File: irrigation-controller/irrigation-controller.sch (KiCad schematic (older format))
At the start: 31 parts, among them P1 CONN_1, P2 CONN_1, P3 CONN_1, P4 CONN_1, P5 CONN_1, P6 CONN_1, P7 CONN_1, P8 CONN_1, P9 PSUBOARD, Q1 IRF540, Q2 IRF540, Q3 IRF540, Q4 IRF540, Q5 IRF540

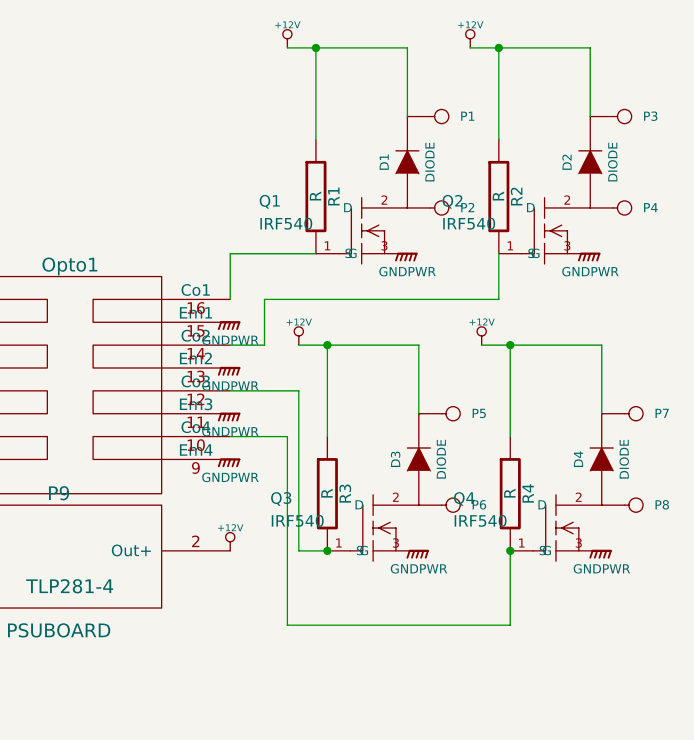
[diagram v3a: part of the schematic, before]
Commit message: Fix inverted behavior on high side
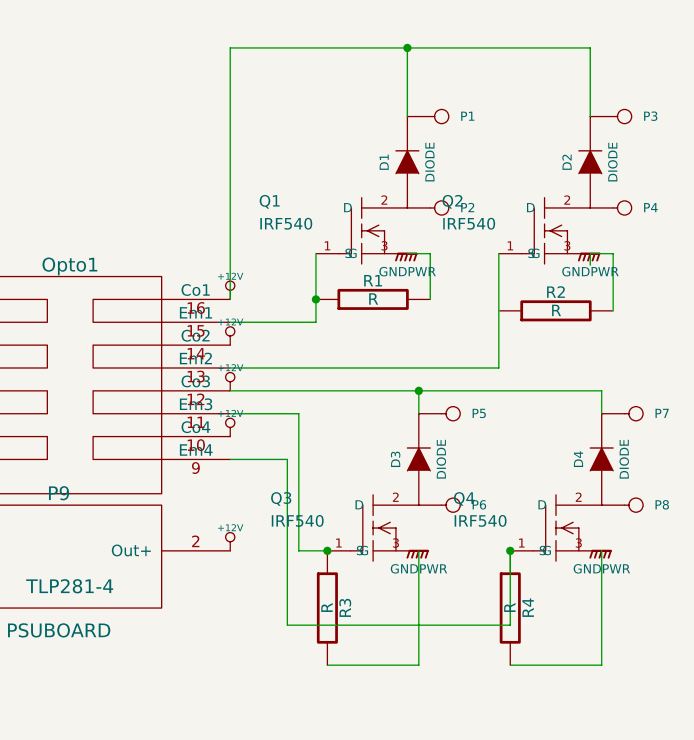
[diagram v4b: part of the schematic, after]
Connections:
- net +12V: now also Opto1.10 (Co4), Opto1.12 (Co3), Opto1.14 (Co2), Opto1.16 (Co1); no longer R1.1, R2.1, R3.1, R4.1
- net GNDPWR: now also R1.2, R2.2, R3.2, R4.2; no longer Opto1.11 (Em3), Opto1.13 (Em2), Opto1.15 (Em1), Opto1.9 (Em4)
- new net: Opto1.15 (Em1), Q1.1 (G), R1.1
- new net: Opto1.11 (Em3), Q3.1 (G), R3.1
- new net: Opto1.13 (Em2), Q2.1 (G)
- new net: Opto1.9 (Em4), Q4.1 (G), R4.1
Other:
- moved on the sheet: R1, R2, R3, R4
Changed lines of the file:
@@
-EESchema Schematic File Version 2  date 5/14/2014 8:58:33 PM
+EESchema Schematic File Version 2  date 6/8/2014 10:10:39 PM
 LIBS:power
 LIBS:device
@@
 Sheet 1 1
 Title ""
-Date "15 may 2014"
+Date "9 jun 2014"
 Rev ""
 Comp ""
@@
 Comment4 ""
 $EndDescr
-$Comp
-L GNDPWR #PWR?
-U 1 1 53741138
-P 9450 3650
-F 0 "#PWR?" H 9450 3700 40  0001 C CNN
-F 1 "GNDPWR" H 9450 3570 40  0000 C CNN
-	1    9450 3650
-	1    0    0    -1
-$EndComp
-$Comp
-L GNDPWR #PWR?
-U 1 1 53741137
-P 9450 3450
-F 0 "#PWR?" H 9450 3500 40  0001 C CNN
-F 1 "GNDPWR" H 9450 3370 40  0000 C CNN
-	1    9450 3450
-	1    0    0    -1
-$EndComp
-$Comp
-L GNDPWR #PWR?
-U 1 1 53741135
-P 9450 3250
-F 0 "#PWR?" H 9450 3300 40  0001 C CNN
-F 1 "GNDPWR" H 9450 3170 40  0000 C CNN
-	1    9450 3250
-	1    0    0    -1
-$EndComp
-$Comp
-L GNDPWR #PWR?
-U 1 1 53741133
-P 9450 3050
-F 0 "#PWR?" H 9450 3100 40  0001 C CNN
-F 1 "GNDPWR" H 9450 2970 40  0000 C CNN
-	1    9450 3050
+Wire Wire Line
+	10325 2950 10325 2750
+Wire Wire Line
+	10325 2750 10225 2750
+Wire Wire Line
+	9450 3050 9825 3050
+Wire Wire Line
+	11025 2800 11025 2750
+Connection ~ 10275 3350
+Wire Wire Line
+	10275 3350 10275 3450
+Wire Wire Line
+	10275 4050 10275 4550
+Wire Wire Line
+	10275 4550 9875 4550
+Wire Wire Line
+	9450 3450 9750 3450
+Wire Wire Line
+	9750 3450 9750 4050
+Wire Wire Line
+	7550 3750 7550 3700
+Wire Wire Line
+	7550 3700 6800 3700
+Wire Wire Line
+	7200 3500 6800 3500
+Wire Wire Line
+	7200 3300 6800 3300
+Wire Wire Line
+	7700 3400 7850 3400
+Wire Wire Line
+	7700 3600 8050 3600
+Wire Wire Line
+	6800 3800 7050 3800
+Wire Wire Line
+	7050 3800 7050 4600
+Wire Wire Line
+	7800 2950 7800 3300
+Wire Wire Line
+	7800 2950 8050 2950
+Wire Wire Line
+	7900 3350 7900 3500
+Wire Wire Line
+	7900 3350 8050 3350
+Connection ~ 9875 4050
+Connection ~ 10675 4050
+Wire Wire Line
+	10675 4050 10675 4375
+Wire Wire Line
+	10225 1850 10225 2150
+Wire Wire Line
+	11025 2150 11025 1850
+Wire Wire Line
+	10675 4375 9700 4375
+Wire Wire Line
+	9750 4050 9875 4050
+Wire Wire Line
+	8050 3600 8050 3550
+Wire Wire Line
+	7850 3400 7850 3150
+Wire Wire Line
+	7850 3150 8050 3150
+Wire Wire Line
+	7050 4600 6800 4600
+Wire Wire Line
+	6800 3900 6950 3900
+Wire Wire Line
+	6950 3900 6950 4500
+Wire Wire Line
+	6950 4500 6800 4500
+Wire Wire Line
+	7900 3500 7700 3500
+Wire Wire Line
+	7800 3300 7700 3300
+Wire Wire Line
+	6800 3400 7200 3400
+Wire Wire Line
+	6800 3600 7200 3600
+Wire Wire Line
+	9450 3650 9700 3650
+Wire Wire Line
+	9700 3650 9700 4375
+Wire Wire Line
+	10675 4550 11075 4550
+Wire Wire Line
+	11075 4550 11075 4050
+Wire Wire Line
+	9450 3350 11075 3350
+Wire Wire Line
+	11075 3350 11075 3450
+Wire Wire Line
+	9450 3250 10625 3250
+Wire Wire Line
+	10625 3250 10625 2750
+Wire Wire Line
+	11125 3000 11125 2750
+Wire Wire Line
+	11125 2750 11025 2750
+Wire Wire Line
+	11025 1850 9450 1850
+Wire Wire Line
+	9450 1850 9450 2950
+Connection ~ 10225 1850
+Wire Wire Line
+	9825 3050 9825 2750
+Connection ~ 9825 2950
+$Comp
+L TLP281-4 Opto1
+U 1 1 5372D520
+P 8750 3500
+F 0 "Opto1" H 8750 4200 60  0000 C CNN
+F 1 "TLP281-4" H 8750 2793 60  0000 C CNN
+	1    8750 3500
 	1    0    0    -1
 $EndComp
@@
 	1    0    0    -1
 $EndComp
-Wire Wire Line
-	7550 3750 7550 3700
-Wire Wire Line
-	7550 3700 6800 3700
-Wire Wire Line
-	7200 3500 6800 3500
-Wire Wire Line
-	7200 3300 6800 3300
-Wire Wire Line
-	7700 3400 7850 3400
-Wire Wire Line
-	7700 3600 8050 3600
-Wire Wire Line
-	6800 3800 7050 3800
-Wire Wire Line
-	7050 3800 7050 4600
-Wire Wire Line
-	7800 2950 7800 3300
-Wire Wire Line
-	7800 2950 8050 2950
-Wire Wire Line
-	7900 3350 7900 3500
-Wire Wire Line
-	7900 3350 8050 3350
-Wire Wire Line
-	9450 3150 9600 3150
-Wire Wire Line
-	9600 3150 9600 2950
-Wire Wire Line
-	9600 2950 10625 2950
-Wire Wire Line
-	10625 2950 10625 2750
-Connection ~ 9875 4050
-Connection ~ 10675 4050
-Wire Wire Line
-	10675 4050 10675 4375
-Wire Wire Line
-	10225 2150 10225 1850
-Wire Wire Line
-	10225 1850 9700 1850
-Wire Wire Line
-	9825 2250 9825 1850
-Connection ~ 9825 1850
-Connection ~ 10625 1850
-Wire Wire Line
-	10625 2250 10625 1850
-Wire Wire Line
-	10500 1850 11025 1850
-Wire Wire Line
-	11025 1850 11025 2150
-Wire Wire Line
-	11075 3450 11075 3150
-Wire Wire Line
-	11075 3150 10550 3150
-Wire Wire Line
-	10675 3550 10675 3150
-Connection ~ 10675 3150
-Connection ~ 9875 3150
-Wire Wire Line
-	9875 3550 9875 3150
-Wire Wire Line
-	9750 3150 10275 3150
-Wire Wire Line
-	10275 3150 10275 3450
-Wire Wire Line
-	9450 3550 9700 3550
-Wire Wire Line
-	9700 3550 9700 4375
-Wire Wire Line
-	9700 4375 10675 4375
-Wire Wire Line
-	9875 4050 9750 4050
-Wire Wire Line
-	9750 4050 9750 3350
-Wire Wire Line
-	9750 3350 9450 3350
-Wire Wire Line
-	9450 2950 9450 2750
-Wire Wire Line
-	9450 2750 9825 2750
-Wire Wire Line
-	8050 3600 8050 3550
-Wire Wire Line
-	7850 3400 7850 3150
-Wire Wire Line
-	7850 3150 8050 3150
-Wire Wire Line
-	7050 4600 6800 4600
-Wire Wire Line
-	6800 3900 6950 3900
-Wire Wire Line
-	6950 3900 6950 4500
-Wire Wire Line
-	6950 4500 6800 4500
-Wire Wire Line
-	7900 3500 7700 3500
-Wire Wire Line
-	7800 3300 7700 3300
-Wire Wire Line
-	6800 3400 7200 3400
-Wire Wire Line
-	6800 3600 7200 3600
 $Comp
 L R R9
@@
 L +12V #PWR011
 U 1 1 5372D5B3
-P 9750 3150
-F 0 "#PWR011" H 9750 3100 20  0001 C CNN
-F 1 "+12V" H 9750 3250 30  0000 C CNN
-	1    9750 3150
+P 9450 3350
+F 0 "#PWR011" H 9450 3300 20  0001 C CNN
+F 1 "+12V" H 9450 3450 30  0000 C CNN
+	1    9450 3350
 	1    0    0    -1
 $EndComp
@@
 L R R3
 U 1 1 5372D5B2
-P 9875 3800
-F 0 "R3" V 9955 3800 50  0000 C CNN
-F 1 "R" V 9875 3800 50  0000 C CNN
-	1    9875 3800
+P 9875 4300
+F 0 "R3" V 9955 4300 50  0000 C CNN
+F 1 "R" V 9875 4300 50  0000 C CNN
+	1    9875 4300
 	1    0    0    -1
 $EndComp
@@
 L R R4
 U 1 1 5372D5AD
-P 10675 3800
-F 0 "R4" V 10755 3800 50  0000 C CNN
-F 1 "R" V 10675 3800 50  0000 C CNN
-	1    10675 3800
+P 10675 4300
+F 0 "R4" V 10755 4300 50  0000 C CNN
+F 1 "R" V 10675 4300 50  0000 C CNN
+	1    10675 4300
 	1    0    0    -1
 $EndComp
@@
 L +12V #PWR012
 U 1 1 5372D5AC
-P 10550 3150
-F 0 "#PWR012" H 10550 3100 20  0001 C CNN
-F 1 "+12V" H 10550 3250 30  0000 C CNN
-	1    10550 3150
+P 9450 3550
+F 0 "#PWR012" H 9450 3500 20  0001 C CNN
+F 1 "+12V" H 9450 3650 30  0000 C CNN
+	1    9450 3550
 	1    0    0    -1
 $EndComp
@@
 L +12V #PWR013
 U 1 1 5372D5A5
-P 10500 1850
-F 0 "#PWR013" H 10500 1800 20  0001 C CNN
-F 1 "+12V" H 10500 1950 30  0000 C CNN
-	1    10500 1850
+P 9450 3150
+F 0 "#PWR013" H 9450 3100 20  0001 C CNN
+F 1 "+12V" H 9450 3250 30  0000 C CNN
+	1    9450 3150
 	1    0    0    -1
 $EndComp
@@
 L R R2
 U 1 1 5372D5A4
-P 10625 2500
-F 0 "R2" V 10705 2500 50  0000 C CNN
-F 1 "R" V 10625 2500 50  0000 C CNN
-	1    10625 2500
-	1    0    0    -1
+P 10875 3000
+F 0 "R2" V 10955 3000 50  0000 C CNN
+F 1 "R" V 10875 3000 50  0000 C CNN
+	1    10875 3000
+	0    -1   -1   0
 $EndComp
 $Comp
@@
 $EndComp
 $Comp
-L TLP281-4 Opto1
-U 1 1 5372D520
-P 8750 3500
-F 0 "Opto1" H 8750 4200 60  0000 C CNN
-F 1 "TLP281-4" H 8750 2793 60  0000 C CNN
-	1    8750 3500
-	1    0    0    -1
-$EndComp
-$Comp
 L CONN_1 P1
 U 1 1 5372D15D
@@
 L R R1
 U 1 1 5372D15B
-P 9825 2500
-F 0 "R1" V 9905 2500 50  0000 C CNN
-F 1 "R" V 9825 2500 50  0000 C CNN
-	1    9825 2500
-	1    0    0    -1
+P 10075 2950
+F 0 "R1" V 10155 2950 50  0000 C CNN
+F 1 "R" V 10075 2950 50  0000 C CNN
+	1    10075 2950
+	0    -1   -1   0
 $EndComp
 $Comp
 L +12V #PWR022
 U 1 1 5372D15A
-P 9700 1850
-F 0 "#PWR022" H 9700 1800 20  0001 C CNN
-F 1 "+12V" H 9700 1950 30  0000 C CNN
-	1    9700 1850
-	1    0    0    -1
-$EndComp
+P 9450 2950
+F 0 "#PWR022" H 9450 2900 20  0001 C CNN
+F 1 "+12V" H 9450 3050 30  0000 C CNN
+	1    9450 2950
+	1    0    0    -1
+$EndComp
